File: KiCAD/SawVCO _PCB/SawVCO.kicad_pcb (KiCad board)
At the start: 2 copper layers, 81.3 x 55.9 mm, 47 parts, among them J1 PWR_IN, J10 Saw_Out, J2 Liner_FM, J3 PWR_OUT, J4 I_Ref, J5 I_Sink, J6 TP_GND, J7 Sync_In, J8 Saw_Out, J9 Saw_Out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

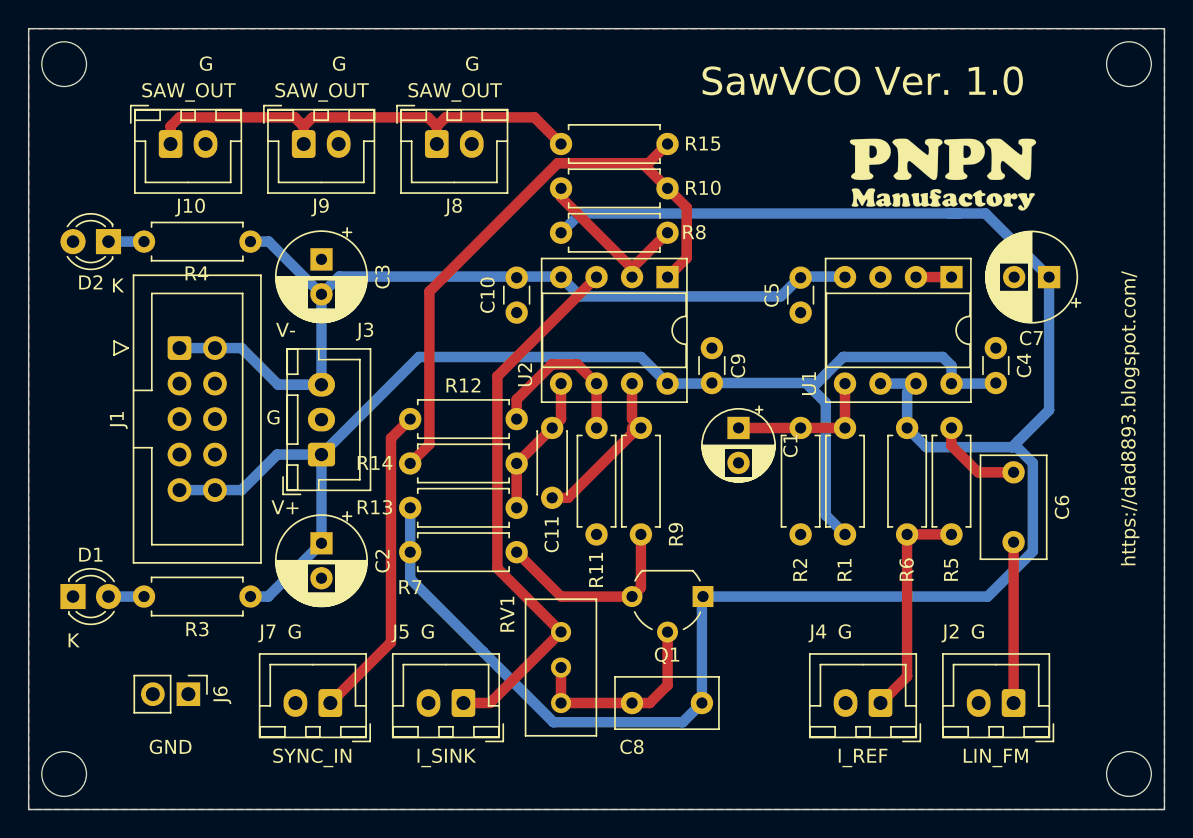
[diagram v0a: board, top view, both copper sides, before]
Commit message: Add +5V Output
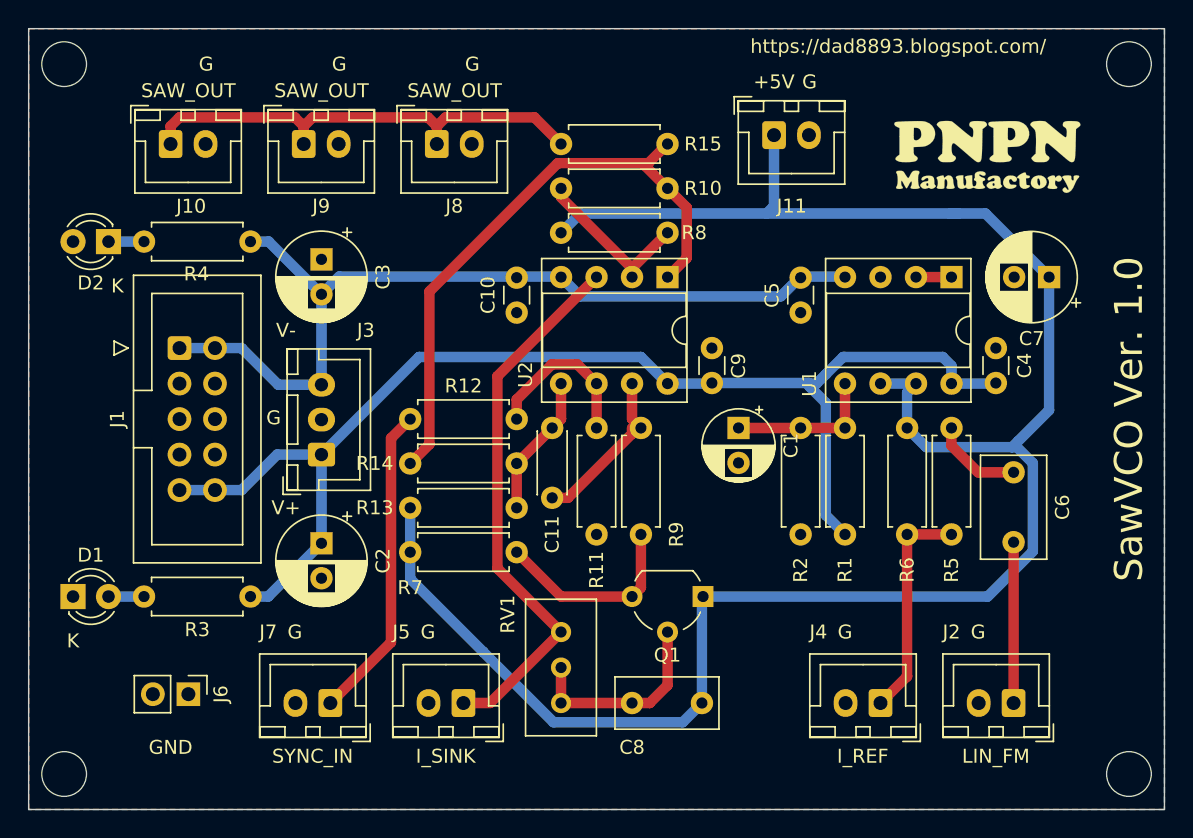
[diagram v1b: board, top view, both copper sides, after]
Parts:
- added J11: +5V, Connector_JST:JST_XH_B2B-XH-A_1x02_P2.50mm_Vertical, F.Cu at (165.1, 78.7)
- moved G*** 3.42 mm to (180.3, 80.0)
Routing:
- net /+5V: track 137.0 -> 142.8 mm
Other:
- board text added: "+5V"

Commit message: 結合テスト
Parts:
- RV1: value 10k -> 5k; footprint Potentiometer_THT:Potentiometer_Bourns_3296W_Vertical -> Potentiometer_THT:Potentiometer_Bourns_3296X_Horizontal
- moved RV1 5.08 mm to (149.9, 114.3), turned to 90 degrees
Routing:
- net Net-(J5-Pad1): track 39.3 -> 41.4 mm
- net Net-(C8-Pad1): track 14.5 -> 15.5 mm
